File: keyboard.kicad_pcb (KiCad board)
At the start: 2 copper layers, 229.6 x 77.2 mm, 348 parts, among them J1 USB_MINI-B, P1 ISP, P2 GPIO_CLUSTER1, P3 GPIO_CLUSTER2, Q1 MOS_P, SW1 MX1A, SW10 MX1A, SW11 MX1A, SW12 MX1A, SW13 MX1A, SW14 MX1A, SW15 MX1A, SW16 MX1A, SW17 MX1A, SW18 MX1A, SW19 MX1A, SW2 MX1A, SW20 MX1A, SW21 MX1A, SW22 MX1A, SW23 MX1A, SW24 MX1A, SW25 MX1A, SW26 MX1A, SW27 MX1A, SW28 MX1A, SW29 MX1A, SW3 MX1A, SW30 MX1A, SW31 MX1A, SW32 MX1A, SW33 MX1A, SW34 MX1A, SW35 MX1A, SW36 MX1A, SW37 MX1A, SW38 MX1A, SW38_625 MX1A, SW39 MX1A, SW4 MX1A, SW40 MX1A, SW41 MX1A, SW42 MX1A, SW5 MX1A, SW6 MX1A, SW7 MX1A, SW8 MX1A, SW9 MX1A, U1 ATMEGA32U4, X1 CRYSTAL

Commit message: Chicory init commit from Daisy
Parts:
- added D43: D_Schottky_Small_ALT, diodes:D_0805_V2, F.Cu at (142.9, 115.3)
- added D44: LED, diodes:D_0805_V2, F.Cu at (142.9, 115.3)
- added J2: Conn_01x02, Connectors_JST:JST_GH_SM02B-GHS-TB_02x1.25mm_Angled, F.Cu at (142.9, 115.3)
- added LED45, LED46: LED, Resistors_SMD:R_0805_HandSoldering, F.Cu at (142.9, 115.3)
- added R10, R11: 2.2K, Resistors_SMD:R_0805_HandSoldering, F.Cu at (142.9, 115.3)
- added R3, R8: 100K, resistors:R_0805_V1, F.Cu at (142.9, 115.3)
- added R9: 1K, resistors:R_0805_V1, F.Cu at (142.9, 115.3)
- added U2: SPX3819M5-L-3-3, TO_SOT_Packages_SMD:SOT-23-5, F.Cu at (142.9, 115.3)
- added U3: MDBT40, mdbt40_carrier:ADA_MDBT40, F.Cu at (142.9, 115.3)
- added U4: MCP73831, TO_SOT_Packages_SMD:SOT-23-5_HandSoldering, F.Cu at (142.9, 115.3)
- C5: value 1uF -> 10uf
- C6, C7, C8: value 100nF -> 10uf
- P2: value GPIO_CLUSTER1 -> CONN_01X03; footprint connectors:Socket_Strip_Straight_2x04_Pitch2.54mm -> connectors:Socket_Strip_Straight_1x03_Pitch2.54mm
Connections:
- net /led/Backlight renamed /Backlight
- net /led/CapsLock renamed /Caps
- net /led/Esc renamed /Esc
- net /led/RGB renamed /RGB
- net /matrix/Col0 renamed /Col0
- net /matrix/Col1 renamed /Col1
- net /matrix/Col10 renamed /Col10
- net /matrix/Col2 renamed /Col2
- net /matrix/Col3 renamed /Col3
- net /matrix/Col4 renamed /Col4
- net /matrix/Col5 renamed /Col5
- net /matrix/Col6 renamed /Col6
- net /matrix/Col7 renamed /Col7
- net /matrix/Col8 renamed /Col8
- net /matrix/Col9 renamed /Col9
- net /matrix/Row0 renamed /Row0
- net /matrix/Row1 renamed /Row1
- net /matrix/Row2 renamed /Row2
- net /matrix/Row3 renamed /Row3
- C5 pad 1: VCC -> VBUS
- C8 pad 1: VCC -> +BATT
- J1 pad 1: VCC -> VBUS
- P2 pad 1: VCC -> Net-(P2-Pad1)
- P2 pad 2: /GPIO0 -> Net-(P2-Pad2)
- P2 pad 3: /GPIO1 -> Net-(P2-Pad3)
- SW38_625 pad HOLE: Net-(D39-Pad1) -> (no net)
- U1 pad : GND -> (no net)
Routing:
- net VCC: track 726.2 -> 564.5 mm, vias 11 -> 8
- net VBUS: track 0.00 -> 79.9 mm, vias 0 -> 1
- net Net-(P2-Pad1): track 0.00 -> 71.1 mm, vias 0 -> 2
- net +BATT: track 0.00 -> 10.7 mm
- net /GPIO3: track 127.7 -> 126.0 mm
- net /GPIO1: track 130.4 -> 128.6 mm
- net Net-(P2-Pad3): track 0.00 -> 1.80 mm
- net Net-(P2-Pad2): track 0.00 -> 1.80 mm

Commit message: 2017年10月29日
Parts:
- removed the SHIELD at (236.2, 53.3)
- removed the SHIELD at (218.4, 63.2)
- removed the SHIELD at (222.6, 61.6)
- removed the SHIELD at (227.3, 56.8)
- removed the SHIELD at (224.8, 51.1)
- C11, C12, C13, C18: footprint capacitors:C_0805_V2 -> capacitors:C_0805
- C14, C15, C16, C17: footprint capacitors:C_0805_V1 -> capacitors:C_0805
- P2: footprint connectors:Socket_Strip_Straight_1x03_Pitch2.54mm -> connectors:Socket_Strip_Straight_1x04_Pitch2.54mm
- R4, R5: footprint resistors:R_0805 -> resistors:R_0805_V1
- U3: moved to B.Cu
- moved U3 100.5 mm to (227.3, 60.9)
- moved JP6 18.1 mm to (204.5, 55.9)
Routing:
- net VCC: track 564.5 -> 677.0 mm, vias 8 -> 11
- net VBUS: track 79.9 -> 7.26 mm, vias 1 -> 0
- net Net-(P2-Pad1): track 71.1 -> 0.00 mm, vias 2 -> 0
- net /GPIO1: track 128.6 -> 87.4 mm
- net /GPIO2: track 125.1 -> 84.8 mm
- net /GPIO3: track 126.0 -> 85.9 mm
- net /GPIO0: track 88.8 -> 52.6 mm
- net /GPIO4: track 92.4 -> 56.6 mm
- net GND: track 767.3 -> 779.0 mm, vias 12 -> 13
- net /led/LRow1: track 201.1 -> 209.9 mm, vias 0 -> 2
- net +BATT: track 10.7 -> 4.03 mm
- net /Row1: track 266.1 -> 269.9 mm
- net Net-(P2-Pad3): track 1.80 -> 0.00 mm
- net Net-(P2-Pad2): track 1.80 -> 0.00 mm

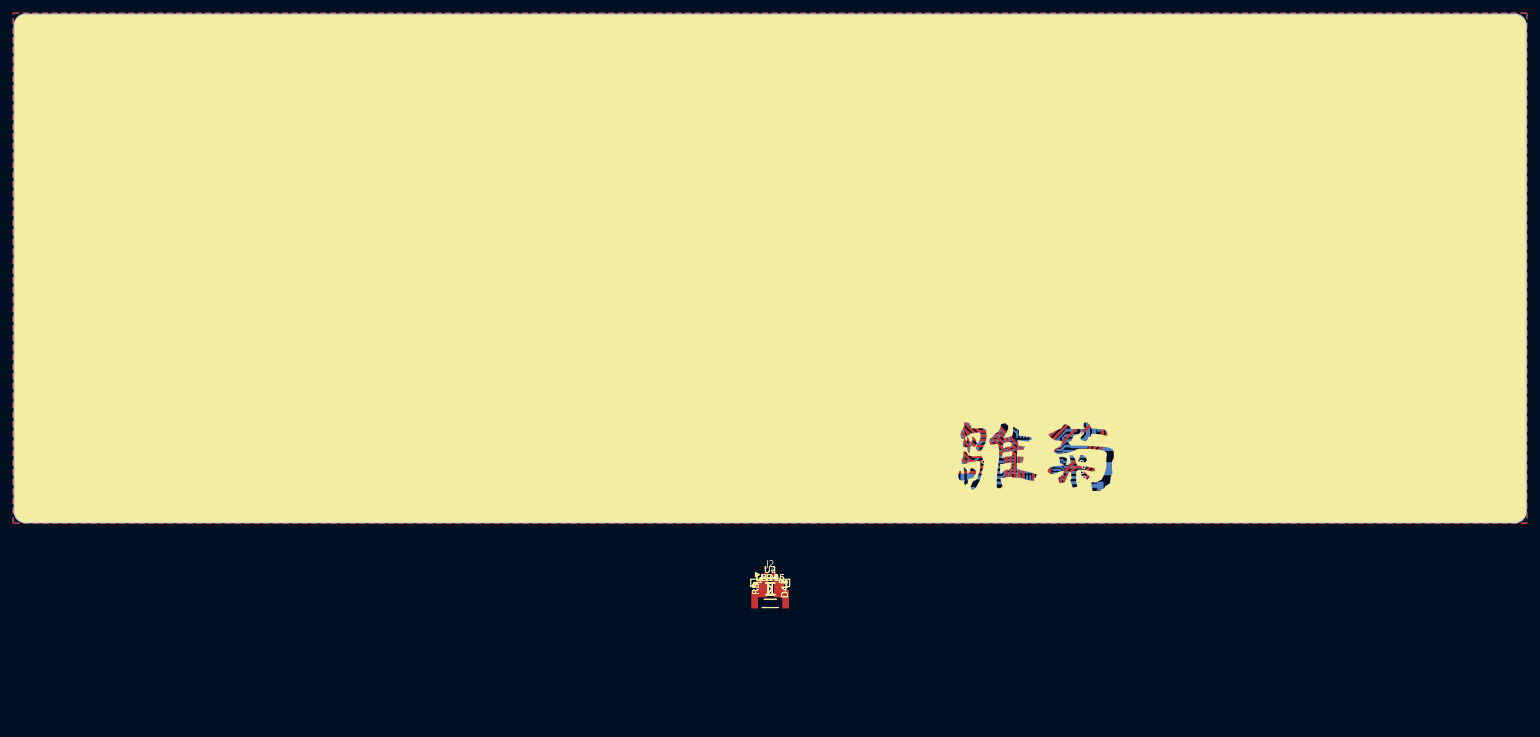
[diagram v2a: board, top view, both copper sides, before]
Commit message: complete without ble led
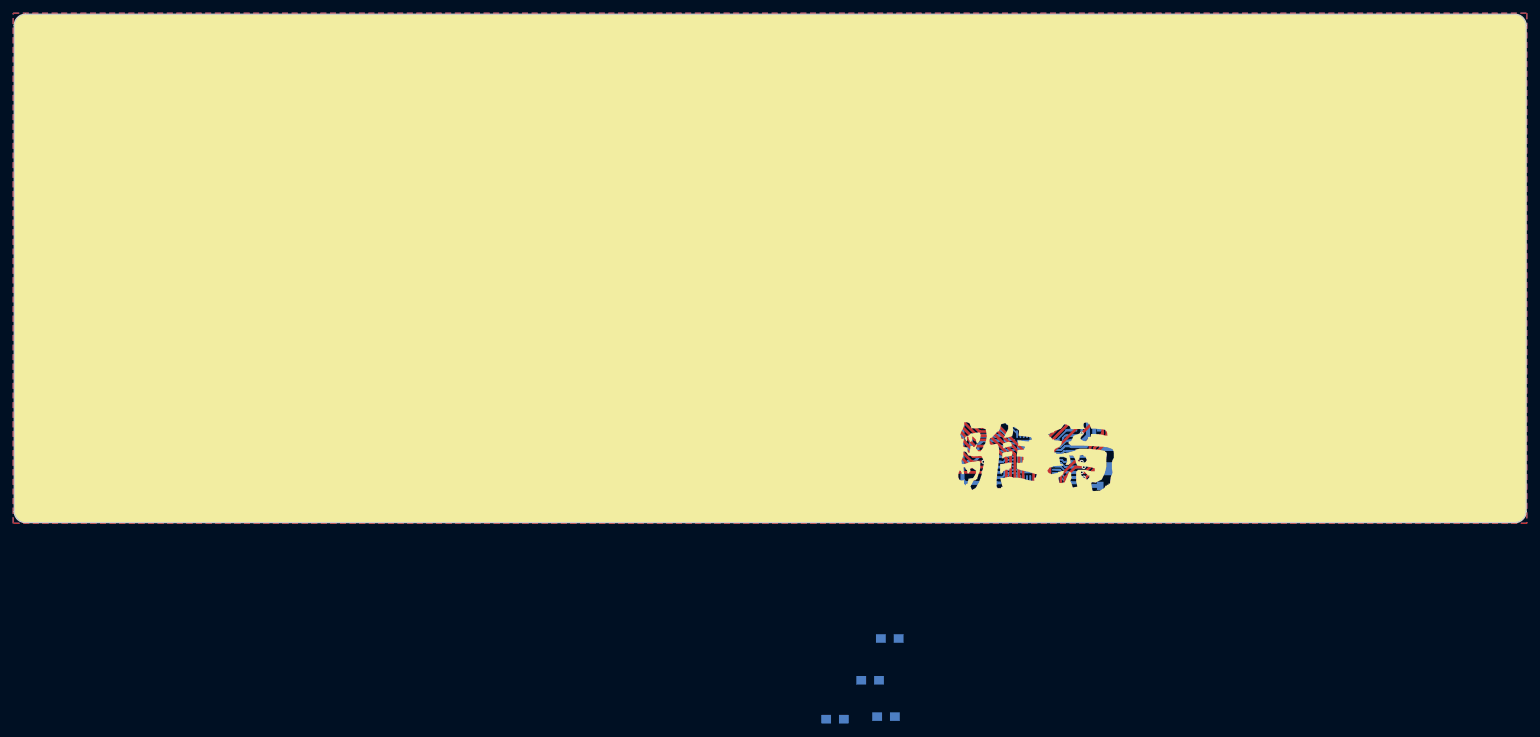
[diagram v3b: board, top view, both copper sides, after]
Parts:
- removed C10, C9: 100nF, capacitors:C_0805
- removed DA1: WE05-4RVLCH, diodes:SOT-23-6_Handsoldering
- removed the SHIELD at (193.7, 44.8)
- removed the SHIELD at (174.6, 44.8)
- removed the SHIELD at (155.6, 44.8)
- removed the SHIELD at (218.1, 70.2)
- removed the SHIELD at (139.1, 42.5)
- removed the SHIELD at (146.7, 42.5)
- D43, D44, J2, LED45, LED46, R10, R11, R3, R8, R9, U2: moved to B.Cu
- U4: footprint TO_SOT_Packages_SMD:SOT-23-5_HandSoldering -> TO_SOT_Packages_SMD:SOT-23-5; moved to B.Cu
- moved J2 92.5 mm to (200.4, 42.9), turned to 270 degrees
- moved D43 82.0 mm to (182.9, 43.8)
- moved R3 80.9 mm to (180.5, 43.7), turned to 90 degrees
- moved U2 79.7 mm to (177.7, 43.7), turned to 180 degrees
- moved D44 77.4 mm to (166.4, 41.5), turned to 270 degrees
- moved R9 76.9 mm to (164.5, 41.5), turned to 270 degrees
- moved U4 76.1 mm to (161.6, 41.5), turned to 180 degrees
- moved R8 75.5 mm to (158.9, 41.5), turned to 90 degrees
- moved C7 71.9 mm to (141.0, 39.9), turned to 90 degrees
- moved C8 58.8 mm to (185.2, 43.8), turned to 270 degrees
- moved C6 58.5 mm to (142.9, 39.9), turned to 90 degrees
- moved C5 50.3 mm to (144.7, 39.9), turned to 90 degrees
- moved LED45 26.2 mm to (160.5, 134.7)
- moved R10 22.1 mm to (152.7, 135.1)
- moved R11 20.6 mm to (158.1, 129.2)
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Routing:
- net VBUS: track 7.26 -> 61.0 mm
- net /Col10: track 171.3 -> 119.2 mm, vias 3 -> 2
- net +BATT: track 4.03 -> 54.3 mm, vias 0 -> 2
- net GND: track 779.0 -> 824.1 mm, vias 13 -> 20
- net Net-(P2-Pad3): track 0.00 -> 43.6 mm, vias 0 -> 2
- net Net-(P2-Pad1): track 0.00 -> 34.4 mm
- net Net-(P2-Pad2): track 0.00 -> 28.8 mm
- net VCC: track 677.0 -> 699.8 mm, vias 11 -> 13
- net /GPIO2: track 84.8 -> 105.5 mm, vias 3 -> 5
- net /GPIO4: track 56.6 -> 75.8 mm, vias 2 -> 4
- net /GPIO3: track 85.9 -> 104.0 mm, vias 3 -> 5
- net /GPIO1: track 87.4 -> 102.8 mm, vias 3 -> 5
- net /GPIO0: track 52.6 -> 63.1 mm
- net /led/LRow1: track 209.9 -> 201.1 mm, vias 2 -> 0
- net /Row1: track 269.9 -> 266.1 mm
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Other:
- board text added: "DFU"
- board text added: "SWC"
- board text added: "SWD"
- board text removed: "PE6"
- board text removed: "SS"

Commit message: complete without bat switch
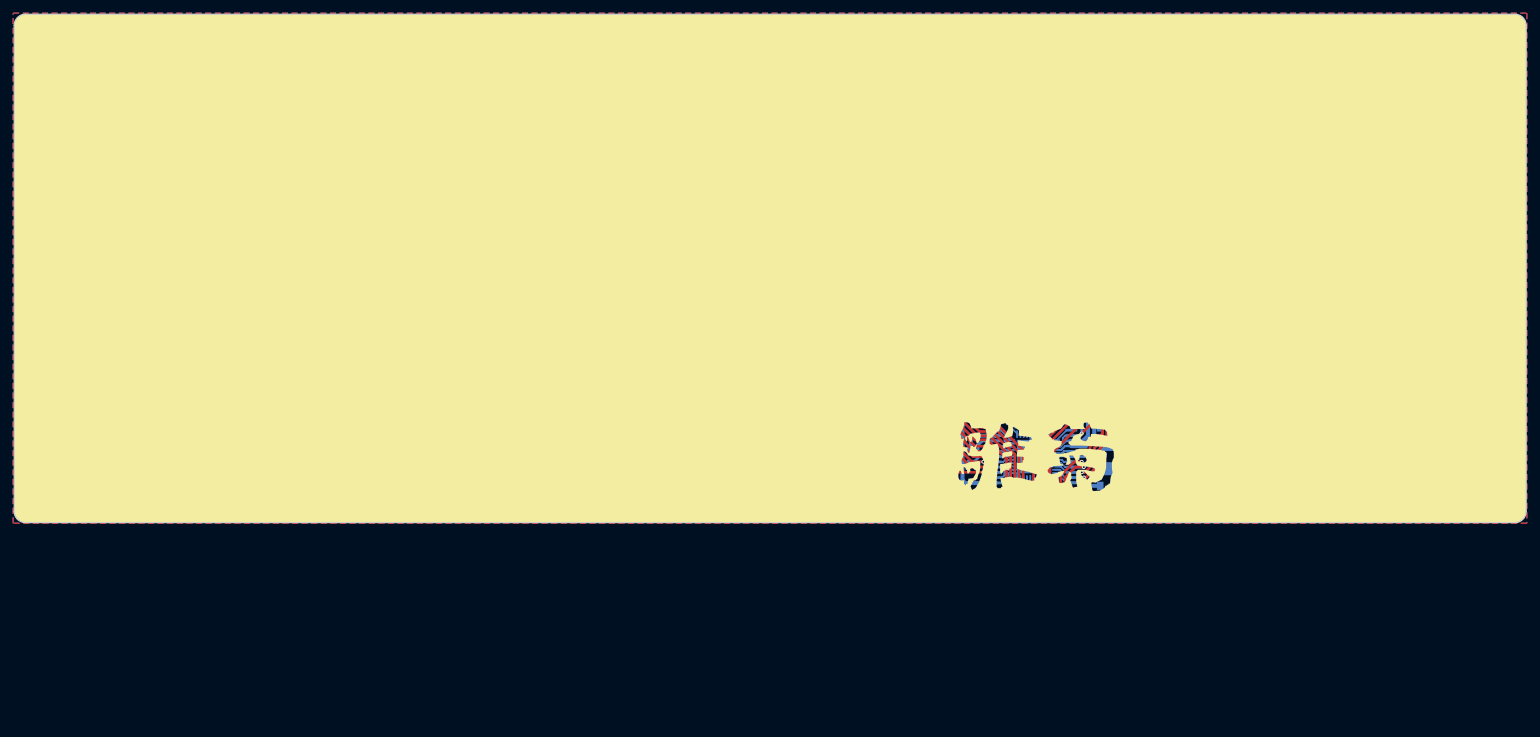
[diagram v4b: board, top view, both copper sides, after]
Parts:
- removed the SHIELD at (216.2, 80.6)
- removed the SHIELD at (244.8, 63.2)
- removed the SHIELD at (208.3, 74.6)
- removed the SHIELD at (220.0, 78.1)
- removed the SHIELD at (218.8, 80.3)
- removed the SHIELD at (231.1, 82.5)
- removed the SHIELD at (239.4, 70.2)
- removed the SHIELD at (241.6, 78.1)
- removed the SHIELD at (161.9, 38.1)
- added SHIELD: Via_0.6mm, passives:Via_0.6mm, F.Cu at (253.0, 81.5)
- added SHIELD: Via_0.6mm, passives:Via_0.6mm, F.Cu at (174.7, 50.0)
- added SHIELD: Via_0.6mm, passives:Via_0.6mm, F.Cu at (149.5, 50.9)
- added SHIELD: Via_0.6mm, passives:Via_0.6mm, F.Cu at (158.9, 44.3)
- added SHIELD: Via_0.6mm, passives:Via_0.6mm, F.Cu at (220.3, 58.8)
- added SHIELD: Via_0.6mm, passives:Via_0.6mm, F.Cu at (228.9, 61.6)
- added SHIELD: Via_0.6mm, passives:Via_0.6mm, F.Cu at (229.0, 56.3)
- added SHIELD: Via_0.6mm, passives:Via_0.6mm, F.Cu at (185.9, 40.1)
- added SHIELD: Via_0.6mm, passives:Via_0.6mm, F.Cu at (180.5, 37.7)
- added SHIELD: Via_0.6mm, passives:Via_0.6mm, F.Cu at (161.8, 36.6)
- added SHIELD: Via_0.6mm, passives:Via_0.6mm, F.Cu at (208.7, 74.6)
- added SHIELD: Via_0.6mm, passives:Via_0.6mm, F.Cu at (207.8, 70.3)
- added SHIELD: Via_0.6mm, passives:Via_0.6mm, F.Cu at (231.6, 89.3)
- added SHIELD: Via_0.6mm, passives:Via_0.6mm, F.Cu at (206.7, 60.1)
- added SHIELD: Via_0.6mm, passives:Via_0.6mm, F.Cu at (139.6, 39.7)
- added SHIELD: Via_0.6mm, passives:Via_0.6mm, F.Cu at (146.2, 39.9)
- added SHIELD: Via_0.6mm, passives:Via_0.6mm, F.Cu at (155.6, 50.0)
- added SHIELD: Via_0.6mm, passives:Via_0.6mm, F.Cu at (193.7, 50.1)
- moved R10 106.6 mm to (235.7, 68.2)
- moved LED45 104.0 mm to (240.4, 68.2), turned to 180 degrees
- moved R11 97.6 mm to (235.6, 70.0)
- moved LED46 95.4 mm to (240.4, 70.0), turned to 180 degrees
- moved C7 39.5 mm to (180.5, 40.8), turned to 0 degrees
- moved C5 38.4 mm to (183.0, 42.9), turned to 0 degrees
- moved C6 37.7 mm to (180.5, 39.1), turned to 0 degrees
- moved C8 23.7 mm to (162.1, 38.5), turned to 180 degrees
- moved J2 2.16 mm to (200.5, 40.7), turned to 180 degrees
- moved D43 0.76 mm to (182.9, 44.5)
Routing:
- net GND: track 824.1 -> 902.4 mm, vias 20 -> 21
- net /Col10: track 119.2 -> 173.7 mm, vias 2 -> 3
- net +BATT: track 54.3 -> 69.2 mm, vias 2 -> 3
- net Net-(R11-Pad1): track 0.00 -> 13.0 mm, vias 0 -> 2
- net Net-(R10-Pad1): track 0.00 -> 10.4 mm, vias 0 -> 2
- net VCC: track 699.8 -> 697.0 mm
- net VBUS: track 61.0 -> 58.6 mm
- net Net-(LED46-Pad2): track 0.00 -> 2.09 mm
- net Net-(LED45-Pad2): track 0.00 -> 2.00 mm
- net Net-(P2-Pad3): track 43.6 -> 42.2 mm, vias 2 -> 1

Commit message: v0.1 complete
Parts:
- removed the SHIELD at (212.7, 44.8)
- added SHIELD: Via_0.6mm, passives:Via_0.6mm, F.Cu at (209.3, 43.8)
- added SHIELD: Via_0.6mm, passives:Via_0.6mm, F.Cu at (201.1, 36.9)
- added SW43: DIP-TOGGLE-SWITCH(3P-9X3.5MM), switches:toggle, B.Cu at (219.9, 43.0)
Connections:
- J2 pad 1: +BATT -> Net-(J2-Pad1)
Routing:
- net Net-(J2-Pad1): track 0.00 -> 24.4 mm
- net +BATT: track 69.2 -> 84.6 mm
